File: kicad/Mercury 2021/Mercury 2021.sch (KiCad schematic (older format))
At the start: 0 parts

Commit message: Updated new board
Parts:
- added C1, C2: 10μf, symbol Device:C
- added J1: Batt_Power, symbol Connector:Screw_Terminal_01x02
- added J10, J11, J12, J13, J2, J3, J4, J5, J6, J9: Screw_Terminal_01x02, symbol Connector:Screw_Terminal_01x02
- added J14, J7, J8: Conn_01x11_Male, symbol Connector:Conn_01x11_Male
- added U1: LM1084-5.0, symbol Regulator_Linear:LM1084-5.0
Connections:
- new net +5V: C2.2, J2.2 (Pin_2), J3.2 (Pin_2), J4.2 (Pin_2), J5.2 (Pin_2), J6.2 (Pin_2), J7.1 (Pin_1), J7.10 (Pin_10), J7.11 (Pin_11), J7.2 (Pin_2), J7.3 (Pin_3), J7.4 (Pin_4), J7.5 (Pin_5), J7.6 (Pin_6), J7.7 (Pin_7), J7.8 (Pin_8), J7.9 (Pin_9), U1.2 (VO)
- new net +BATT: C1.1, J1.2 (Pin_2), J10.1 (Pin_1), J11.1 (Pin_1), J12.1 (Pin_1), J13.1 (Pin_1), J14.1 (Pin_1), J14.10 (Pin_10), J14.11 (Pin_11), J14.2 (Pin_2), J14.3 (Pin_3), J14.4 (Pin_4), J14.5 (Pin_5), J14.6 (Pin_6), J14.7 (Pin_7), J14.8 (Pin_8), J14.9 (Pin_9), J9.1 (Pin_1), U1.3 (VI)
- new net GND: C1.2, C2.1, J1.1 (Pin_1), J10.2 (Pin_2), J11.2 (Pin_2), J12.2 (Pin_2), J13.2 (Pin_2), J2.1 (Pin_1), J3.1 (Pin_1), J4.1 (Pin_1), J5.1 (Pin_1), J6.1 (Pin_1), J8.1 (Pin_1), J8.10 (Pin_10), J8.11 (Pin_11), J8.2 (Pin_2), J8.3 (Pin_3), J8.4 (Pin_4), J8.5 (Pin_5), J8.6 (Pin_6), J8.7 (Pin_7), J8.8 (Pin_8), J8.9 (Pin_9), J9.2 (Pin_2), U1.1 (GND)

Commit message: Updated new board
Created a 3.3v rail
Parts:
- removed C2: 10μf, symbol Device:C
- added C? (x3): 10μf, symbol Device:CP
- added J?: Conn_01x11_Male, symbol Connector:Conn_01x11_Male
- added J? (x5): Screw_Terminal_01x02, symbol Connector:Screw_Terminal_01x02
- added U?: LM1084-3.3, symbol Regulator_Linear:LM1084-3.3
- C1: symbol Device:C -> Device:CP
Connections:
- net +5V: now also J10.1 (Pin_1), J11.1 (Pin_1), J12.1 (Pin_1), J13.1 (Pin_1), J9.1 (Pin_1), C?.1; no longer J2.2 (Pin_2), J3.2 (Pin_2), J4.2 (Pin_2), J5.2 (Pin_2), J6.2 (Pin_2)
- net +BATT: now also C?.1, U?.3 (VI); no longer J10.1 (Pin_1), J11.1 (Pin_1), J12.1 (Pin_1), J13.1 (Pin_1), J9.1 (Pin_1)
- net GND: now also C?.2, J?.2 (Pin_2), J?.2 (Pin_2), J?.2 (Pin_2), J?.2 (Pin_2), J?.2 (Pin_2)
- new net: C?.2, C?.2
- new net +3V3: C?.1, J2.2 (Pin_2), J3.2 (Pin_2), J4.2 (Pin_2), J5.2 (Pin_2), J6.2 (Pin_2), J?.1 (Pin_1), J?.1 (Pin_1), J?.1 (Pin_1), J?.1 (Pin_1), J?.1 (Pin_1), J?.1 (Pin_1), J?.10 (Pin_10), J?.11 (Pin_11), J?.2 (Pin_2), J?.3 (Pin_3), J?.4 (Pin_4), J?.5 (Pin_5), J?.6 (Pin_6), J?.7 (Pin_7), J?.8 (Pin_8), J?.9 (Pin_9), U?.2 (VO)
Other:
- moved on the sheet: J10, J11, J12, J13, J2, J3, J4, J5, J6, J9

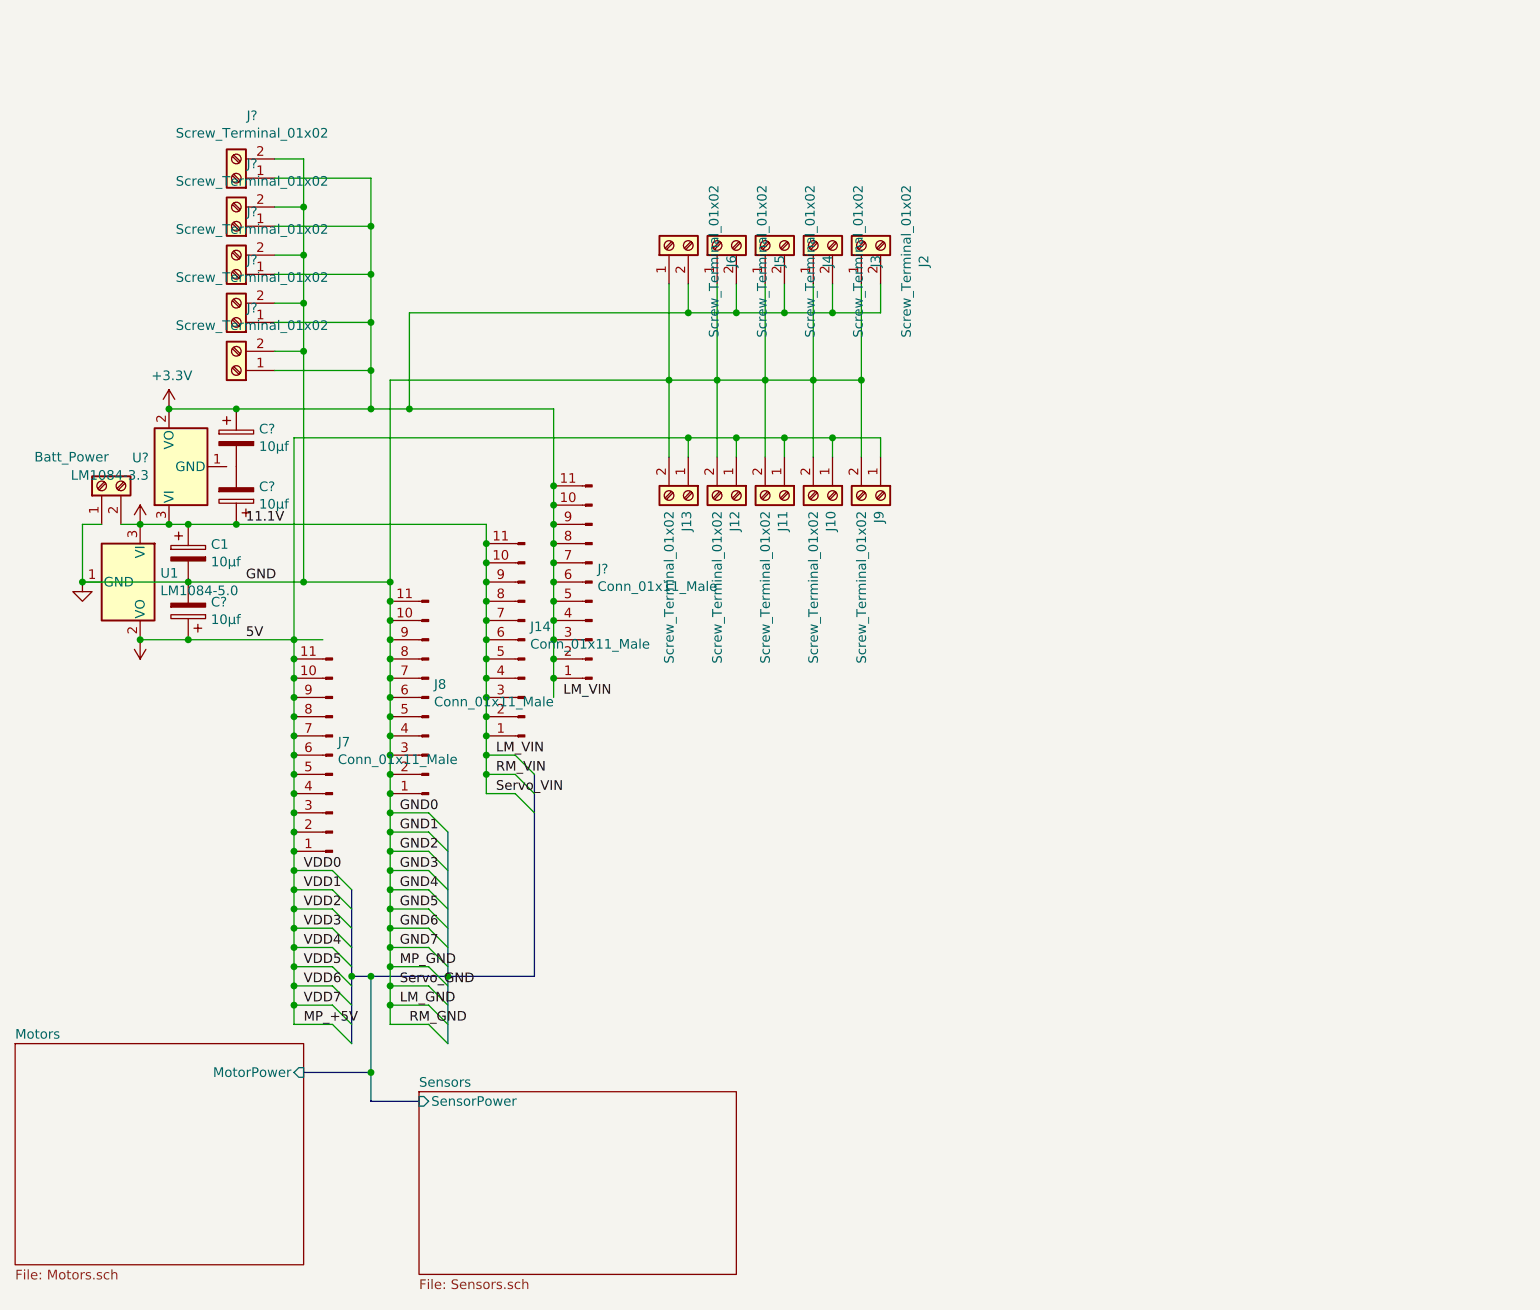
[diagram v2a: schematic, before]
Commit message: Updated the new PCB (lots of notes)
- added net
- changed symbols
- added footprints
- added ability to put the pi -> arduino cable through the board
- fixed global labels
- named connectors
- started adding things to title block

Notes:
- footprints for some parts were chosen at random, connectors need to be chosen on digikey
-- connectors for ribbon cables
-- USB connectors
-- screw terminals
- for these, the footprints may be wrong, so we need to make sure the connectors for them are spaced right
-- arduino
-- servo controller
-- PWM controller
- Board is unorganized, cluttered, and unusable, needs to be managed. considerations:
-- Pins carrying power and data should be separated by distance or GND
-- able to access connectors (not blocked by other things)
- Finish adding things to the title blocks and the PCB silkscreen
-- names or members
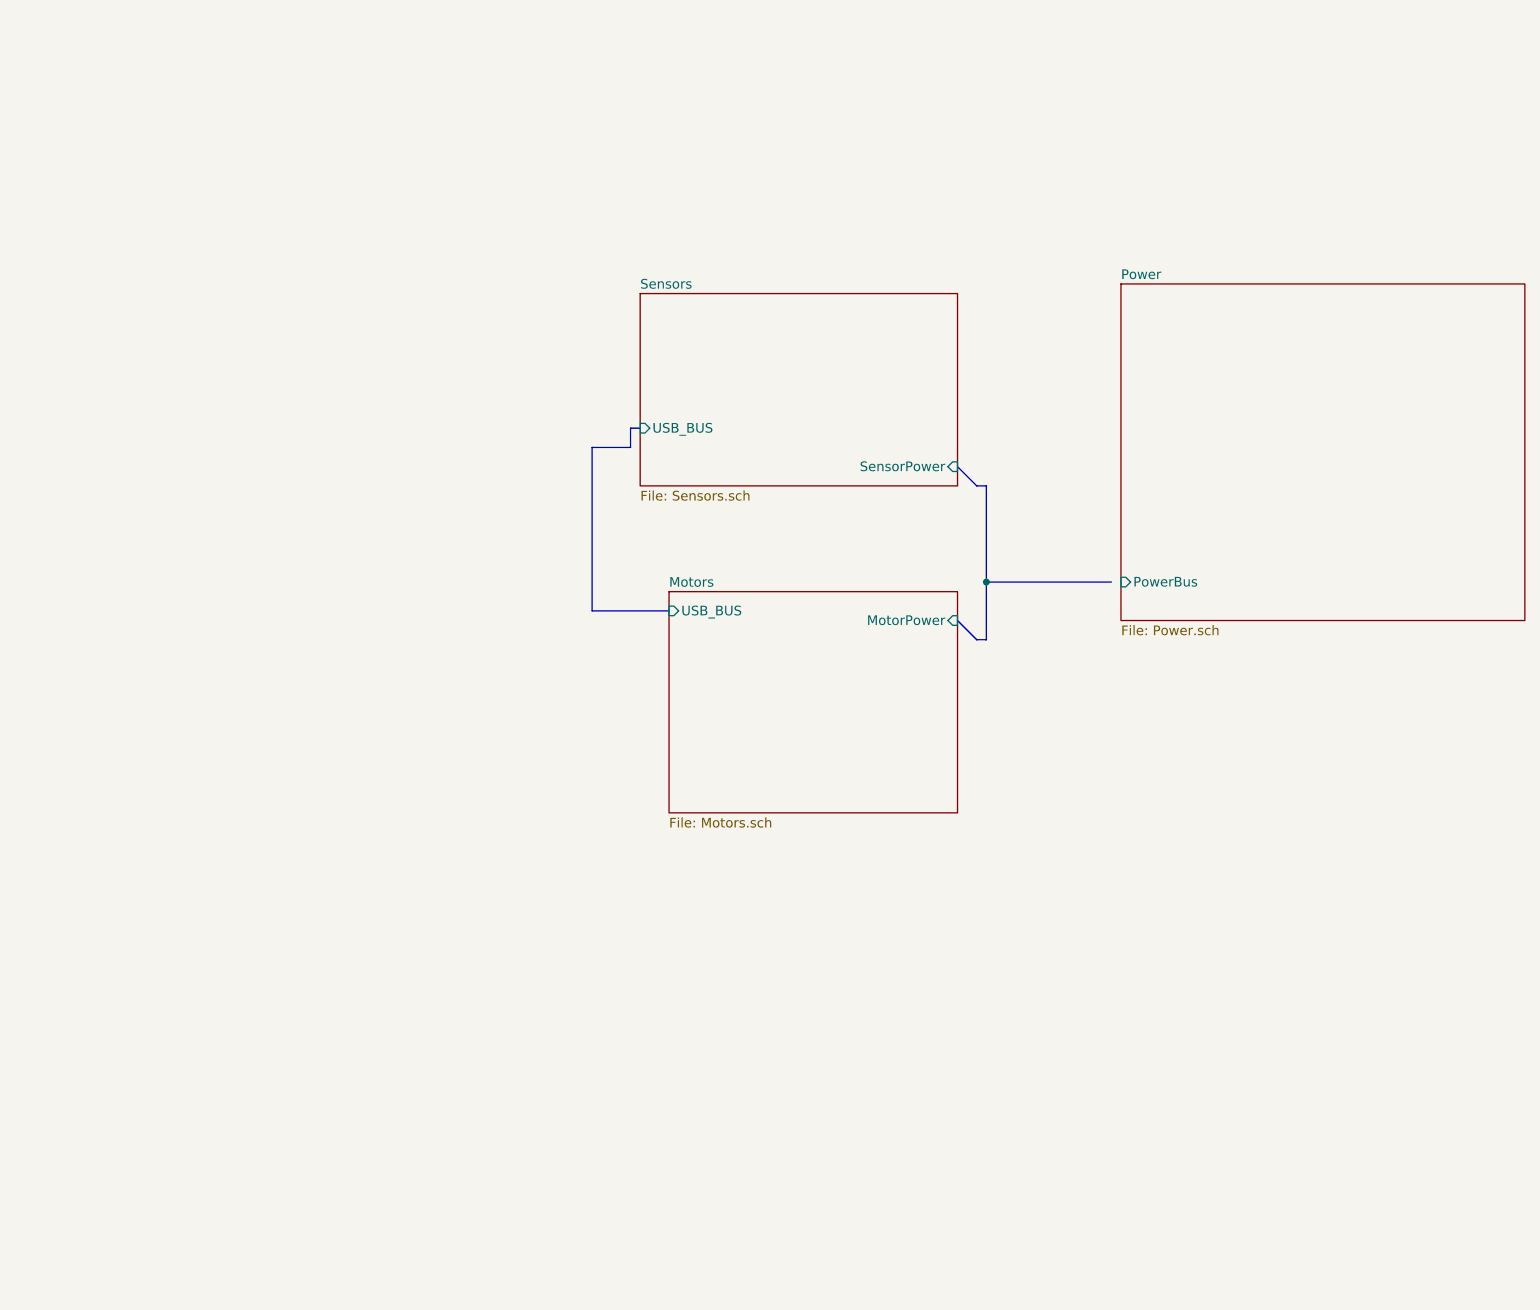
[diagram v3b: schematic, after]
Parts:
- removed C1, C? (x3): 10μf, symbol Device:CP
- removed J1: Batt_Power, symbol Connector:Screw_Terminal_01x02
- removed J10, J11, J12, J13, J2, J3, J4, J5, J6, J9, J? (x5): Screw_Terminal_01x02, symbol Connector:Screw_Terminal_01x02
- removed J14, J7, J8, J?: Conn_01x11_Male, symbol Connector:Conn_01x11_Male
- removed U1: LM1084-5.0, symbol Regulator_Linear:LM1084-5.0
- removed U?: LM1084-3.3, symbol Regulator_Linear:LM1084-3.3

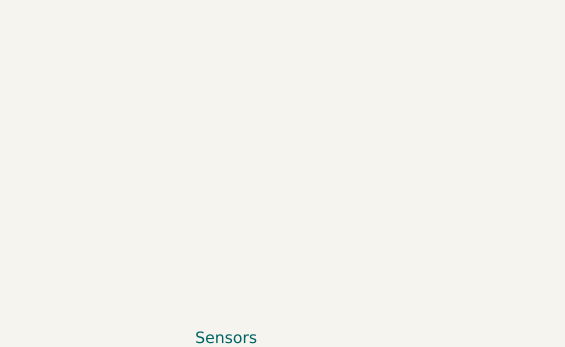
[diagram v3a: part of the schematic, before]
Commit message: Updated board
Silk screen and mounting holes
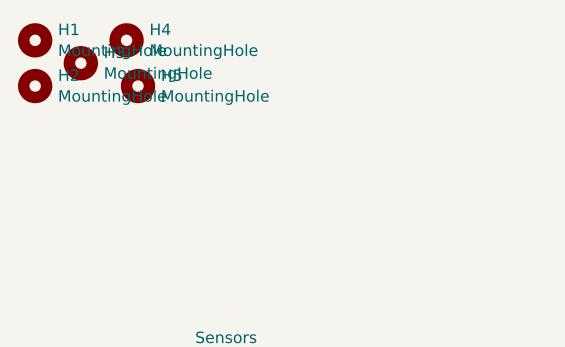
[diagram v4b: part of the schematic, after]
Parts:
- added H1, H2, H3, H4, H5: MountingHole, MountingHole:MountingHole_4.3mm_M4_DIN965_Pad_TopBottom, symbol Mechanical:MountingHole
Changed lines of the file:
@@
 Wire Bus Line
 	4300 3200 4300 3300
+$Comp
+L Mechanical:MountingHole H1
+U 1 1 609FDF60
+P 3650 1150
+F 0 "H1" H 3750 1196 50  0000 L CNN
+F 1 "MountingHole" H 3750 1105 50  0000 L CNN
+F 2 "MountingHole:MountingHole_4.3mm_M4_DIN965_Pad_TopBottom" H 3650 1150 50  0001 C CNN
+F 3 "~" H 3650 1150 50  0001 C CNN
+	1    3650 1150
+	1    0    0    -1
+$EndComp
+$Comp
+L Mechanical:MountingHole H4
+U 1 1 60A0061F
+P 4050 1150
+F 0 "H4" H 4150 1196 50  0000 L CNN
+F 1 "MountingHole" H 4150 1105 50  0000 L CNN
+F 2 "MountingHole:MountingHole_4.3mm_M4_DIN965_Pad_TopBottom" H 4050 1150 50  0001 C CNN
+F 3 "~" H 4050 1150 50  0001 C CNN
+	1    4050 1150
+	1    0    0    -1
+$EndComp
+$Comp
+L Mechanical:MountingHole H2
+U 1 1 60A00807
+P 3650 1350
+F 0 "H2" H 3750 1396 50  0000 L CNN
+F 1 "MountingHole" H 3750 1305 50  0000 L CNN
+F 2 "MountingHole:MountingHole_4.3mm_M4_DIN965_Pad_TopBottom" H 3650 1350 50  0001 C CNN
+F 3 "~" H 3650 1350 50  0001 C CNN
+	1    3650 1350
+	1    0    0    -1
+$EndComp
+$Comp
+L Mechanical:MountingHole H5
+U 1 1 60A00A27
+P 4100 1350
+F 0 "H5" H 4200 1396 50  0000 L CNN
+F 1 "MountingHole" H 4200 1305 50  0000 L CNN
+F 2 "MountingHole:MountingHole_4.3mm_M4_DIN965_Pad_TopBottom" H 4100 1350 50  0001 C CNN
+F 3 "~" H 4100 1350 50  0001 C CNN
+	1    4100 1350
+	1    0    0    -1
+$EndComp
+$Comp
+L Mechanical:MountingHole H3
+U 1 1 60A00CDB
+P 3850 1250
+F 0 "H3" H 3950 1296 50  0000 L CNN
+F 1 "MountingHole" H 3950 1205 50  0000 L CNN
+F 2 "MountingHole:MountingHole_4.3mm_M4_DIN965_Pad_TopBottom" H 3850 1250 50  0001 C CNN
+F 3 "~" H 3850 1250 50  0001 C CNN
+	1    3850 1250
+	1    0    0    -1
+$EndComp
 $EndSCHEMATC
